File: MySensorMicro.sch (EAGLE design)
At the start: 21 parts, among them IC1 MEGA328P-AU, IC2 25AA080SN, IC3 SI7021, IC4 ATSHA204A, Q1 32768hz

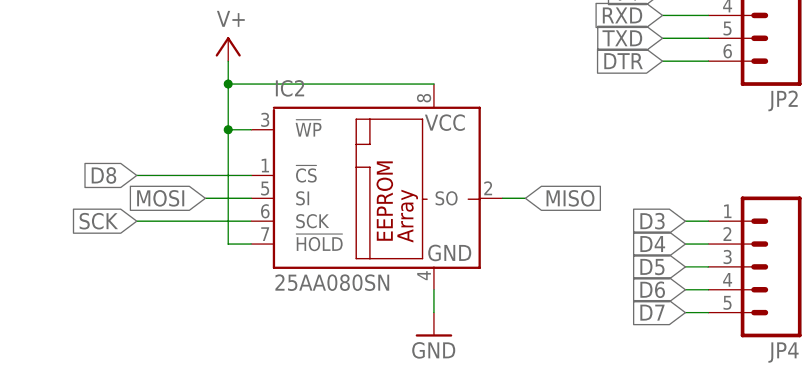
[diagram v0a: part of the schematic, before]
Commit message: Updated part number for external flash
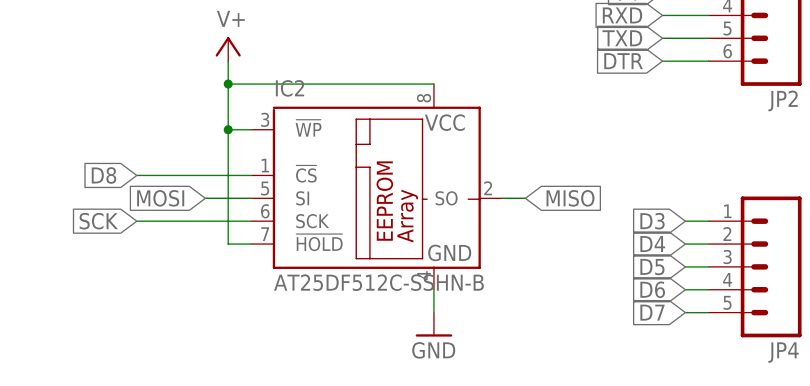
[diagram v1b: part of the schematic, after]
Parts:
- IC2: value 25AA080SN -> AT25DF512C-SSHN-B
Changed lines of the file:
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@@
 <?xml version="1.0" encoding="utf-8"?>
 <!DOCTYPE eagle SYSTEM "eagle.dtd">
-<eagle version="7.1.0">
+<eagle version="7.2.0">
 <drawing>
 <settings>
@@
 <setting verticaltext="up"/>
 </settings>
-<grid distance="0.05" unitdist="inch" unit="inch" style="lines" multiple="1" display="no" altdistance="0.01" altunitdist="inch" altunit="inch"/>
+<grid distance="0.1" unitdist="inch" unit="inch" style="lines" multiple="1" display="no" altdistance="0.01" altunitdist="inch" altunit="inch"/>
 <layers>
 <layer number="1" name="Top" color="4" fill="1" visible="no" active="no"/>
@@
 <part name="C3" library="Discrete" deviceset="CAP" device="-0603" value="4u7"/>
 <part name="SUPPLY1" library="supply2" deviceset="V+" device=""/>
-<part name="IC2" library="microchip" deviceset="25*" device="SN" technology="AA080"/>
+<part name="IC2" library="microchip" deviceset="25*" device="SN" technology="AA080" value="AT25DF512C-SSHN-B"/>
 <part name="GND3" library="supply1" deviceset="GND" device=""/>
 <part name="JP1" library="pinhead" deviceset="PINHD-2X4" device="" value="Radio"/>

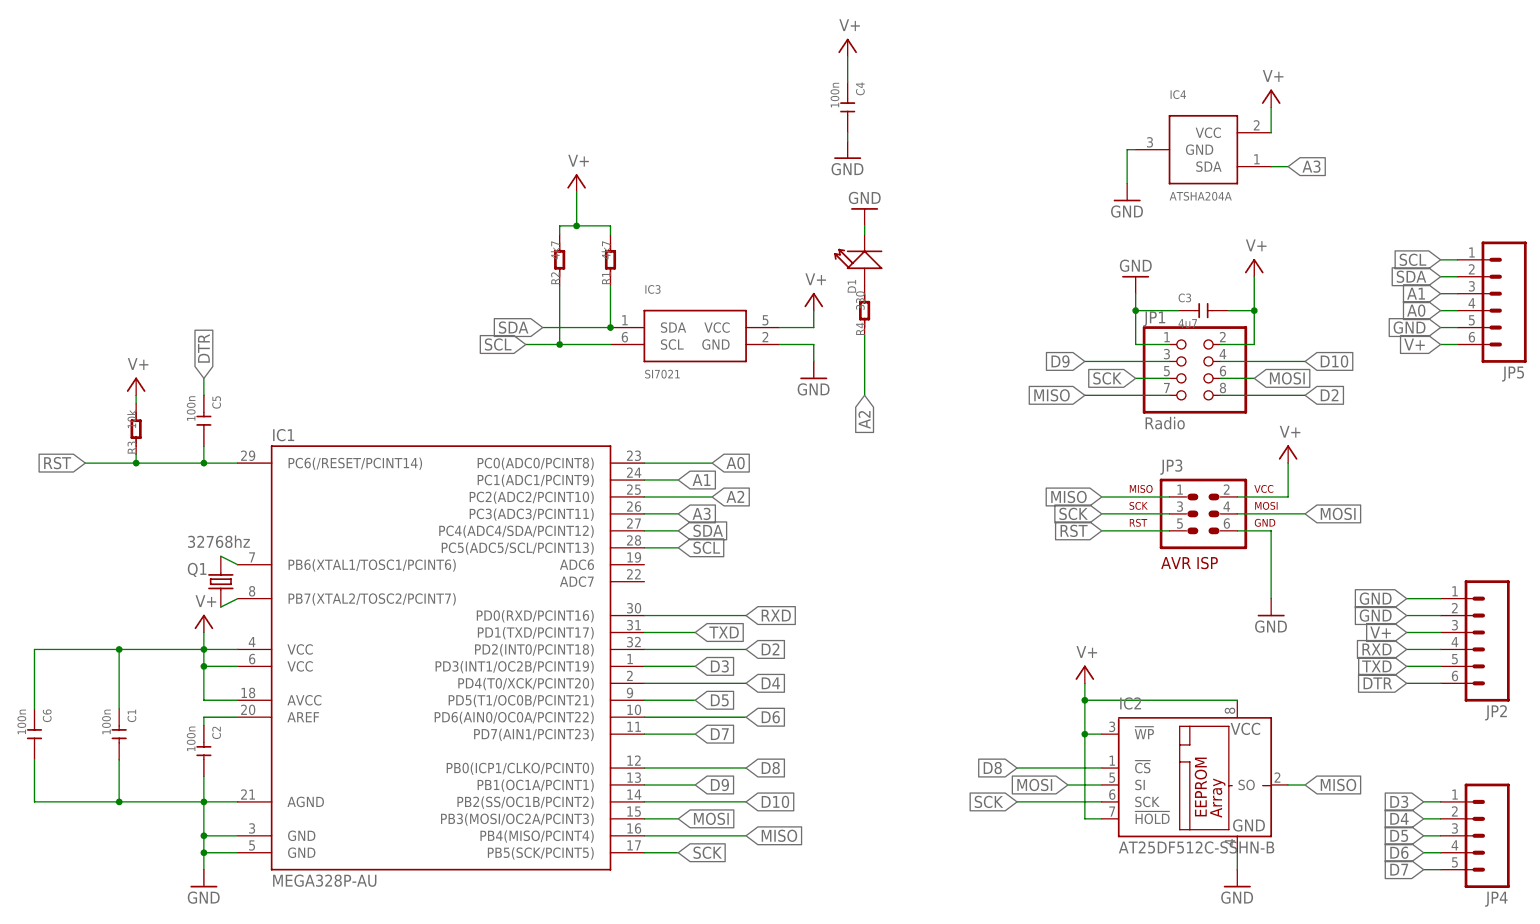
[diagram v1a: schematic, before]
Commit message: Updated with pullup on both CSN on NRF module, and CE on external flash
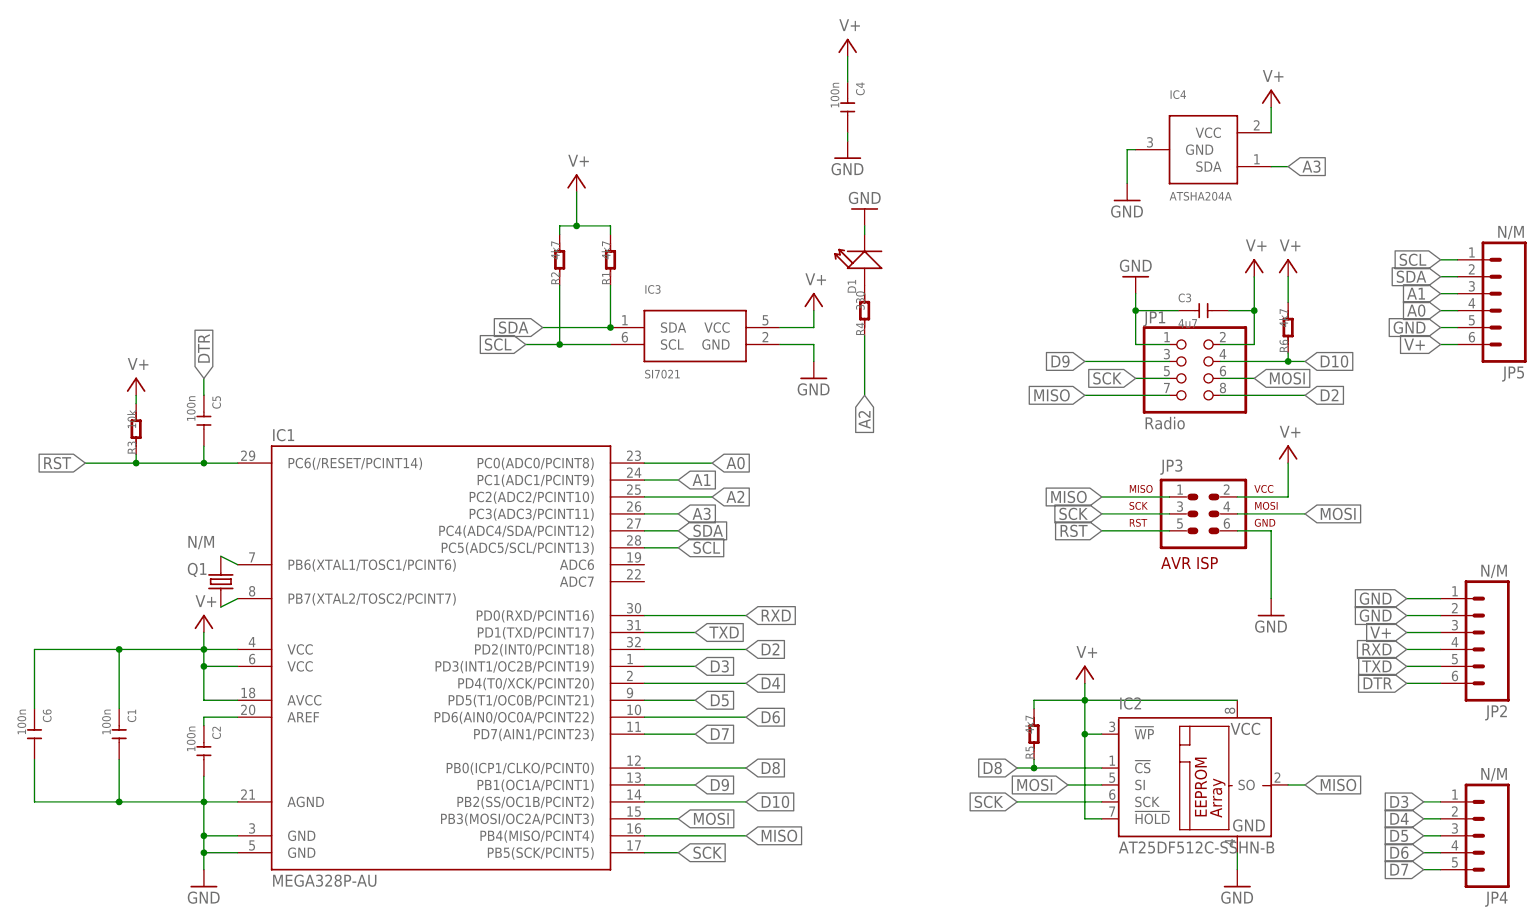
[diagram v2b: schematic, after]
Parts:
- added R5, R6: 4k7, Discrete:R-0402
- JP2, JP4, JP5: value (none) -> N/M
- JP3: value AVR-ISP-6VERT -> N/M
- Q1: value 32768hz -> N/M
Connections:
- net D10: now also R6.1
- net D8: now also R5.1
- net V+: now also R5.2, R6.2
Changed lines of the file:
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@@
 <setting verticaltext="up"/>
 </settings>
-<grid distance="0.1" unitdist="inch" unit="inch" style="lines" multiple="1" display="no" altdistance="0.01" altunitdist="inch" altunit="inch"/>
+<grid distance="0.05" unitdist="inch" unit="inch" style="lines" multiple="1" display="no" altdistance="0.01" altunitdist="inch" altunit="inch"/>
 <layers>
 <layer number="1" name="Top" color="4" fill="1" visible="no" active="no"/>
@@
 <part name="GND1" library="supply1" deviceset="GND" device=""/>
 <part name="GND7" library="supply1" deviceset="GND" device=""/>
-<part name="JP3" library="avr-7" deviceset="AVR-ISP-6" device="VERT"/>
+<part name="JP3" library="avr-7" deviceset="AVR-ISP-6" device="VERT" value="N/M"/>
 <part name="GND8" library="supply1" deviceset="GND" device=""/>
 <part name="C2" library="Discrete" deviceset="CAP" device="-0402" value="100n"/>
-<part name="Q1" library="Discrete" deviceset="CRYSTAL*" device="-306010055" value="32768hz"/>
+<part name="Q1" library="Discrete" deviceset="CRYSTAL*" device="-306010055" value="N/M"/>
 <part name="GND4" library="supply1" deviceset="GND" device=""/>
 <part name="SUPPLY3" library="supply2" deviceset="V+" device=""/>
@@
 <part name="GND10" library="supply1" deviceset="GND" device=""/>
 <part name="C4" library="Discrete" deviceset="CAP" device="-0402" value="100n"/>
-<part name="JP2" library="SparkFun-Connectors" deviceset="M06" device="NO_SILK_FEMALE_PTH"/>
+<part name="JP2" library="SparkFun-Connectors" deviceset="M06" device="NO_SILK_FEMALE_PTH" value="N/M"/>
 <part name="C5" library="Discrete" deviceset="CAP" device="-0402" value="100n"/>
-<part name="JP4" library="SparkFun-Connectors" deviceset="M05" device="NO_SILK"/>
-<part name="JP5" library="SparkFun-Connectors" deviceset="M06" device="NO_SILK_FEMALE_PTH"/>
+<part name="JP4" library="SparkFun-Connectors" deviceset="M05" device="NO_SILK" value="N/M"/>
+<part name="JP5" library="SparkFun-Connectors" deviceset="M06" device="NO_SILK_FEMALE_PTH" value="N/M"/>
 <part name="R3" library="Discrete" deviceset="R*" device="-0402" value="10k"/>
 <part name="SUPPLY2" library="supply2" deviceset="V+" device=""/>
@@
 <part name="GND2" library="supply1" deviceset="GND" device=""/>
 <part name="SUPPLY7" library="supply2" deviceset="V+" device=""/>
+<part name="R5" library="Discrete" deviceset="R*" device="-0402" value="4k7"/>
+<part name="R6" library="Discrete" deviceset="R*" device="-0402" value="4k7"/>
+<part name="SUPPLY10" library="supply2" deviceset="V+" device=""/>
 </parts>
 <sheets>
@@
 <instance part="GND2" gate="1" x="161.29" y="118.11"/>
 <instance part="SUPPLY7" gate="1" x="182.88" y="134.62"/>
+<instance part="R5" gate="R" x="147.32" y="38.1" rot="R90"/>
+<instance part="R6" gate="R" x="185.42" y="99.06" rot="R90"/>
+<instance part="SUPPLY10" gate="1" x="185.42" y="109.22"/>
 </instances>
 <busses>
@@
 <junction x="154.94" y="43.18"/>
 <pinref part="SUPPLY6" gate="1" pin="V+"/>
+<wire x1="147.32" y1="43.18" x2="154.94" y2="43.18" width="0.1524" layer="91"/>
+<pinref part="R5" gate="R" pin="2"/>
+<wire x1="147.32" y1="41.91" x2="147.32" y2="43.18" width="0.1524" layer="91"/>
 </segment>
 <segment>
@@
 <pinref part="SUPPLY7" gate="1" pin="V+"/>
 <wire x1="182.88" y1="128.27" x2="182.88" y2="132.08" width="0.1524" layer="91"/>
+</segment>
+<segment>
+<pinref part="R6" gate="R" pin="2"/>
+<pinref part="SUPPLY10" gate="1" pin="V+"/>
+<wire x1="185.42" y1="102.87" x2="185.42" y2="106.68" width="0.1524" layer="91"/>
 </segment>
 </net>
@@
 <segment>
 <pinref part="JP1" gate="A" pin="4"/>
-<wire x1="175.26" y1="93.98" x2="187.96" y2="93.98" width="0.1524" layer="91"/>
+<wire x1="175.26" y1="93.98" x2="185.42" y2="93.98" width="0.1524" layer="91"/>
 <label x="187.96" y="93.98" size="1.778" layer="95" xref="yes"/>
+<pinref part="R6" gate="R" pin="1"/>
+<wire x1="185.42" y1="93.98" x2="187.96" y2="93.98" width="0.1524" layer="91"/>
+<wire x1="185.42" y1="95.25" x2="185.42" y2="93.98" width="0.1524" layer="91"/>
+<junction x="185.42" y="93.98"/>
 </segment>
 </net>
@@
 <segment>
 <pinref part="IC2" gate="G$1" pin="!CS"/>
-<wire x1="157.48" y1="33.02" x2="144.78" y2="33.02" width="0.1524" layer="91"/>
+<wire x1="157.48" y1="33.02" x2="147.32" y2="33.02" width="0.1524" layer="91"/>
 <label x="144.78" y="33.02" size="1.778" layer="95" rot="R180" xref="yes"/>
-</segment>
-</net>
+<pinref part="R5" gate="R" pin="1"/>
+<wire x1="147.32" y1="33.02" x2="144.78" y2="33.02" width="0.1524" layer="91"/>
+<wire x1="147.32" y1="34.29" x2="147.32" y2="33.02" width="0.1524" layer="91"/>
+<junction x="147.32" y="33.02"/>
+</segment>
+</net>

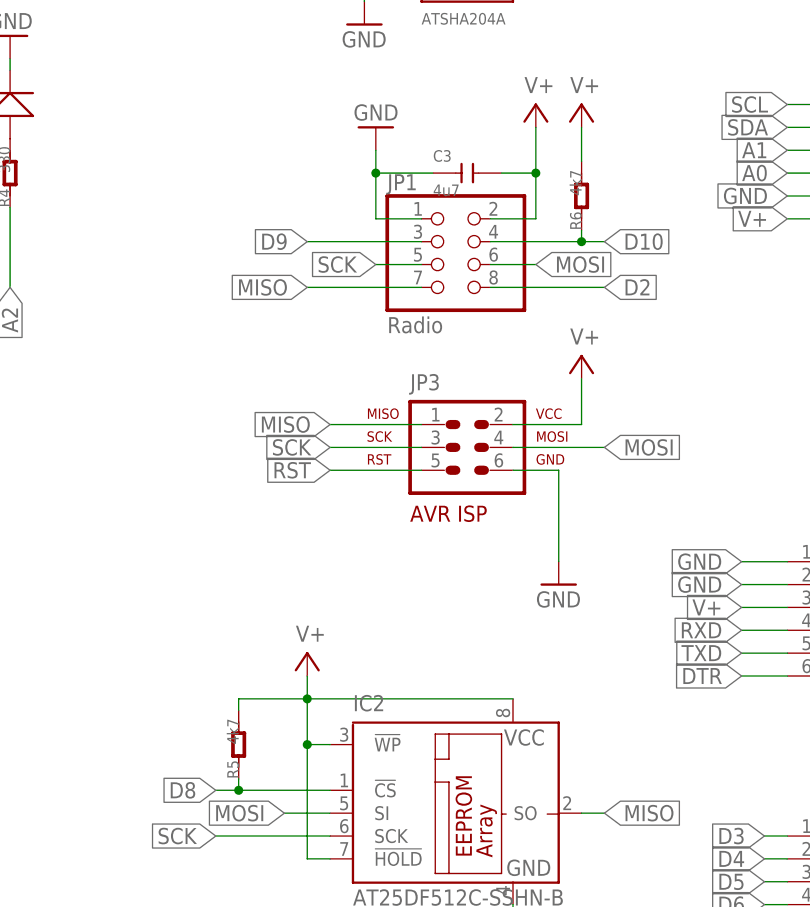
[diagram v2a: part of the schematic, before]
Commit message: Updated component values on R5/R6
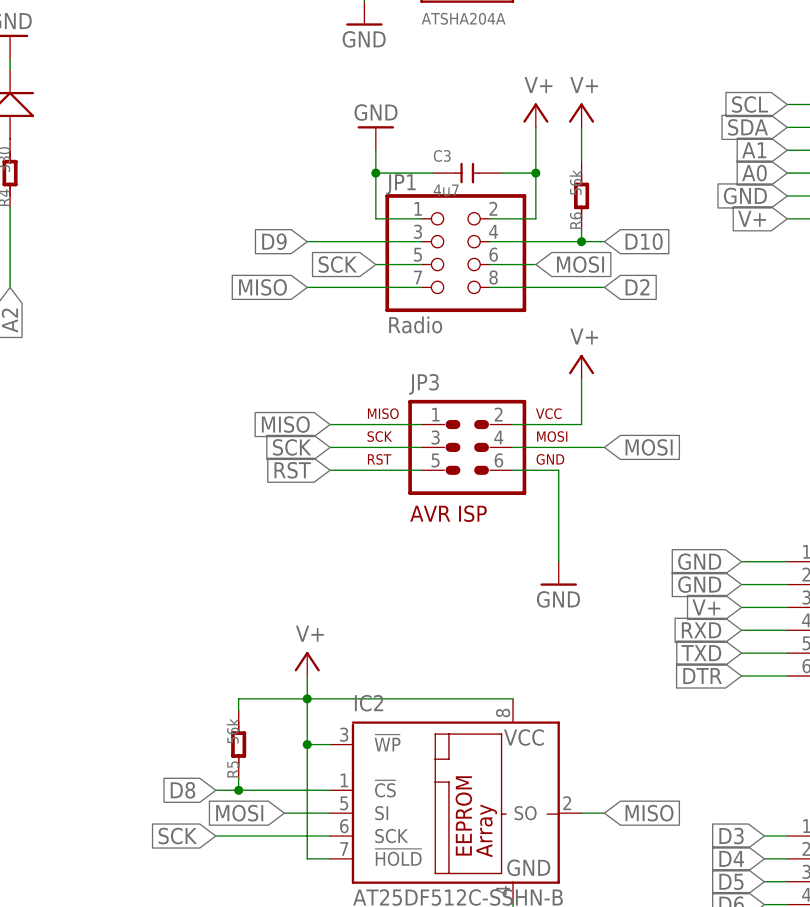
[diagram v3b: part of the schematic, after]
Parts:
- R5, R6: value 4k7 -> 56k
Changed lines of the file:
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@@
 <setting verticaltext="up"/>
 </settings>
-<grid distance="0.05" unitdist="inch" unit="inch" style="lines" multiple="1" display="no" altdistance="0.01" altunitdist="inch" altunit="inch"/>
+<grid distance="0.1" unitdist="inch" unit="inch" style="lines" multiple="1" display="no" altdistance="0.01" altunitdist="inch" altunit="inch"/>
 <layers>
 <layer number="1" name="Top" color="4" fill="1" visible="no" active="no"/>
@@
 <part name="GND2" library="supply1" deviceset="GND" device=""/>
 <part name="SUPPLY7" library="supply2" deviceset="V+" device=""/>
-<part name="R5" library="Discrete" deviceset="R*" device="-0402" value="4k7"/>
-<part name="R6" library="Discrete" deviceset="R*" device="-0402" value="4k7"/>
+<part name="R5" library="Discrete" deviceset="R*" device="-0402" value="56k"/>
+<part name="R6" library="Discrete" deviceset="R*" device="-0402" value="56k"/>
 <part name="SUPPLY10" library="supply2" deviceset="V+" device=""/>
 </parts>
